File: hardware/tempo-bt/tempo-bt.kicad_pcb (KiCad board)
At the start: 4 copper layers, 58.4 x 54 mm, 69 parts, among them J1 JSTPH, J2 USB_C_Receptacle_USB2.0, J3 IO Interfaces, J4 QWIIC_CONNECTORJS-1MM, J5 2x5 PTH ARM CORTEX DEBUG, Q1 DMP3125L, SW1 JS102011SAQN, SW2 UBXH19-0000035, SW3 UBXH19-0000035, SW4 RESET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

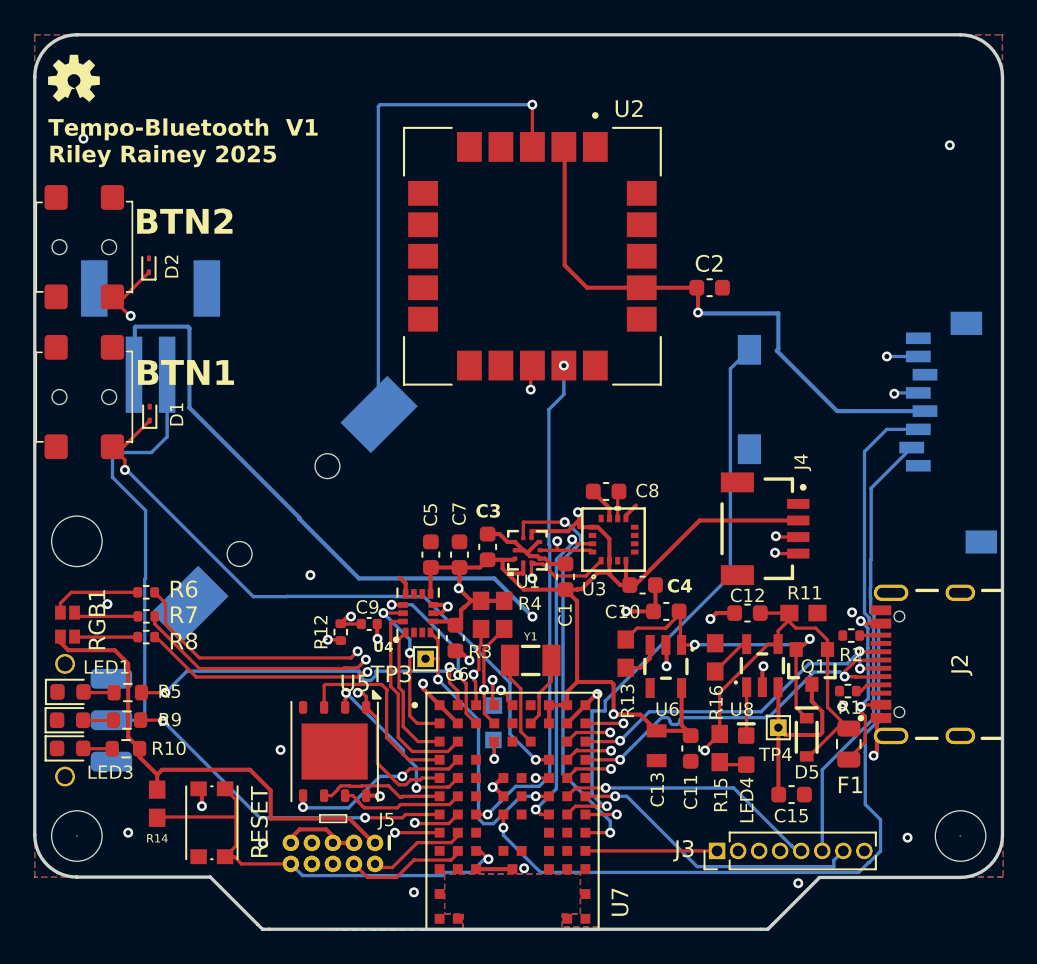
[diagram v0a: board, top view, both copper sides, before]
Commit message: Switch orientation incorrect; fixed
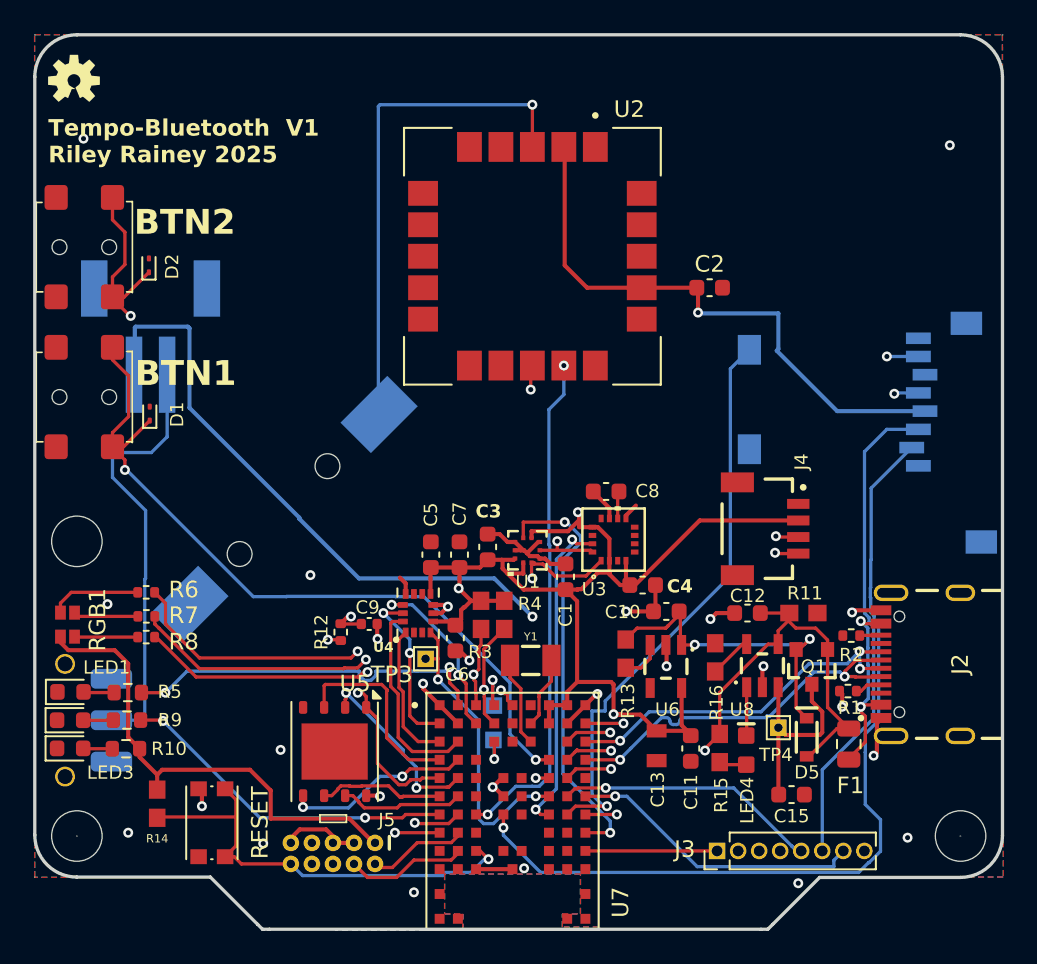
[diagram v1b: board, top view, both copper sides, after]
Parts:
- C9: value UBXH01-2021002100N -> 100nF
- Q1: value DMP3125L -> DMP3125L-7
- R12: value UBXH18-0008113470K -> 470KOHM
- R6: value UBXH18-0000269499R -> 499OHM-0402
- R7, R8: value UBXH18-0008033220R -> 220OHM-0402
- RGB1: value UBXH11-0000058 -> LTST-C19HE1WT
- SW2, SW3: value UBXH19-0000035 -> PTS850
- U5: value UBXH13-0000138 -> MX25R64
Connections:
- SW2 pad 2: unconnected-(SW2-Pad2) -> GND
- SW2 pad 3: GND -> /BTN1
- SW3 pad 2: unconnected-(SW3-Pad2) -> GND
- SW3 pad 3: GND -> /BTN2
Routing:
- net /BTN1: track 39.3 -> 46.1 mm
- net /BTN2: track 51.3 -> 57.9 mm
- net GND: track 40.9 -> 43.9 mm

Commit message: Through Task 5
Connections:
- U2 pad 7: unconnected-(U2-TIMEPULSE-Pad7) -> /GNSS_TIMEPULSE
- U7 pad H3: unconnected-(U7-P0.27/AIN6-PadH3) -> /GNSS_TIMEPULSE
- U7 pad H7: /BTN3 -> unconnected-(U7-P0.29-PadH7)
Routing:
- net /GNSS_TIMEPULSE: track 0.00 -> 46.8 mm, vias 0 -> 3
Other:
- board text added: "Tempo-Bluetooth V2 Riley Rainey 2025"
- board text removed: "Tempo-Bluetooth V1 Riley Rainey 2025"
